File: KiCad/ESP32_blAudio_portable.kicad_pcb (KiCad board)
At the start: 2 copper layers, 102 parts, among them J1 Conn_01x15_Male, J2 Conn_01x15_Male, J3 Conn_01x02_Male, J4 Conn_01x02_Male, J5 Conn_01x02_Male, J7 Conn_01x16_Female, SW1 SW_Push, SW2 SW_Push, SW3 SW_Push, SW5 SW_Push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

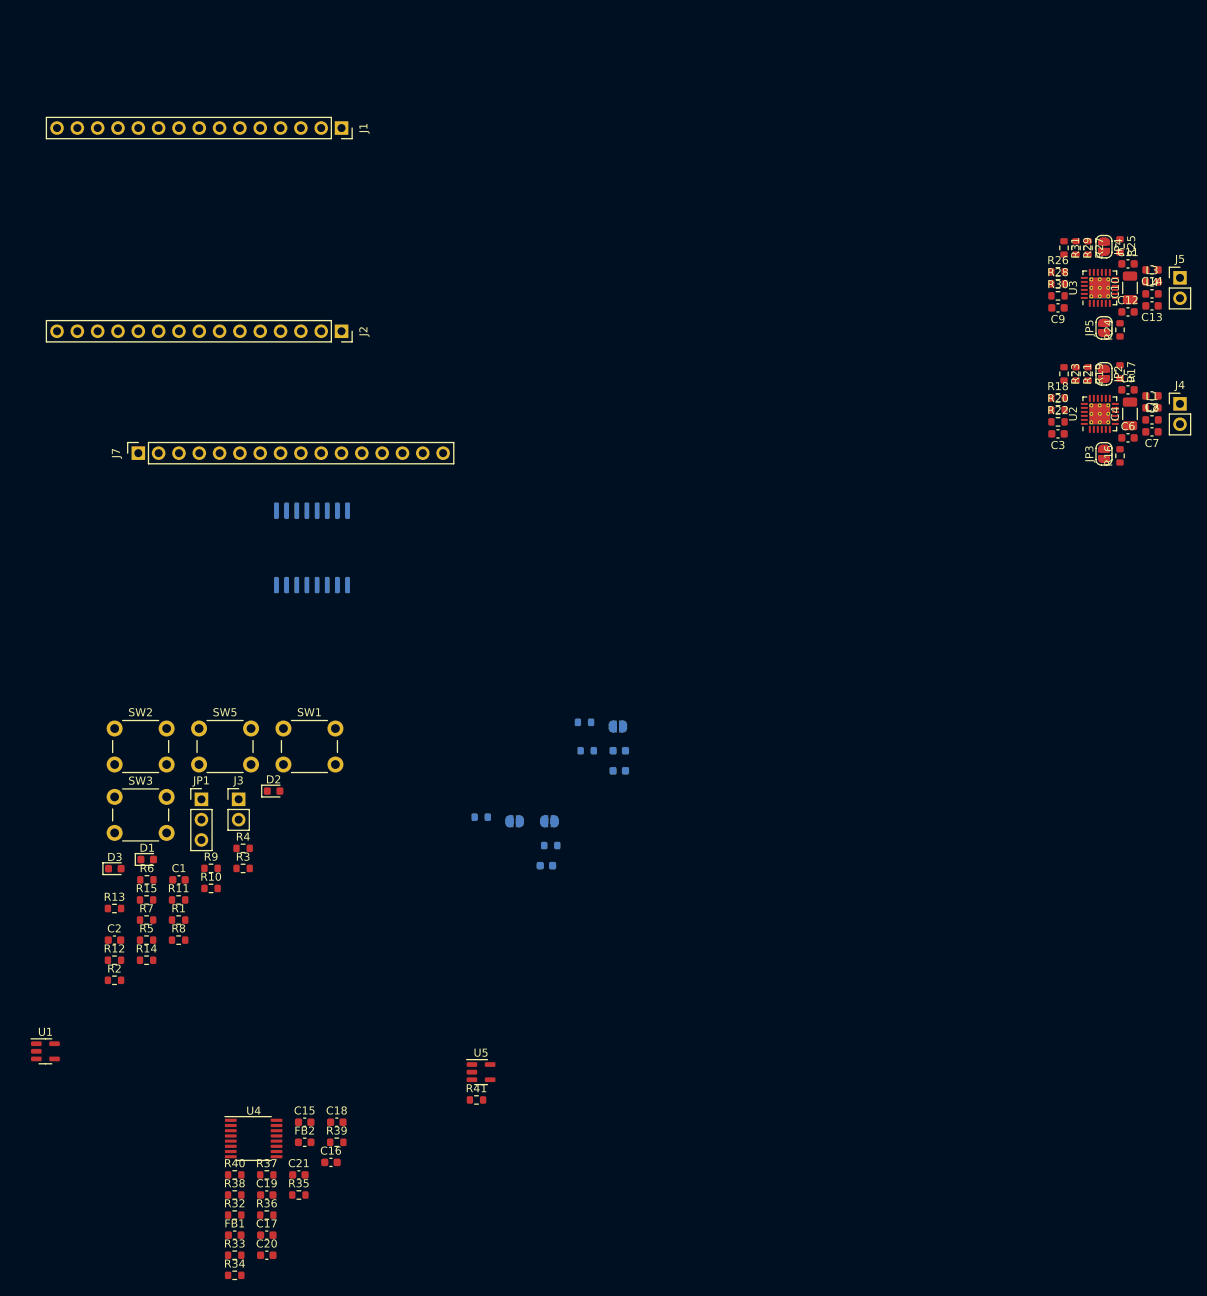
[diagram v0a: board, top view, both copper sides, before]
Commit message: -associated footprints to more specific components -added manufacturer and part series info to more specific components
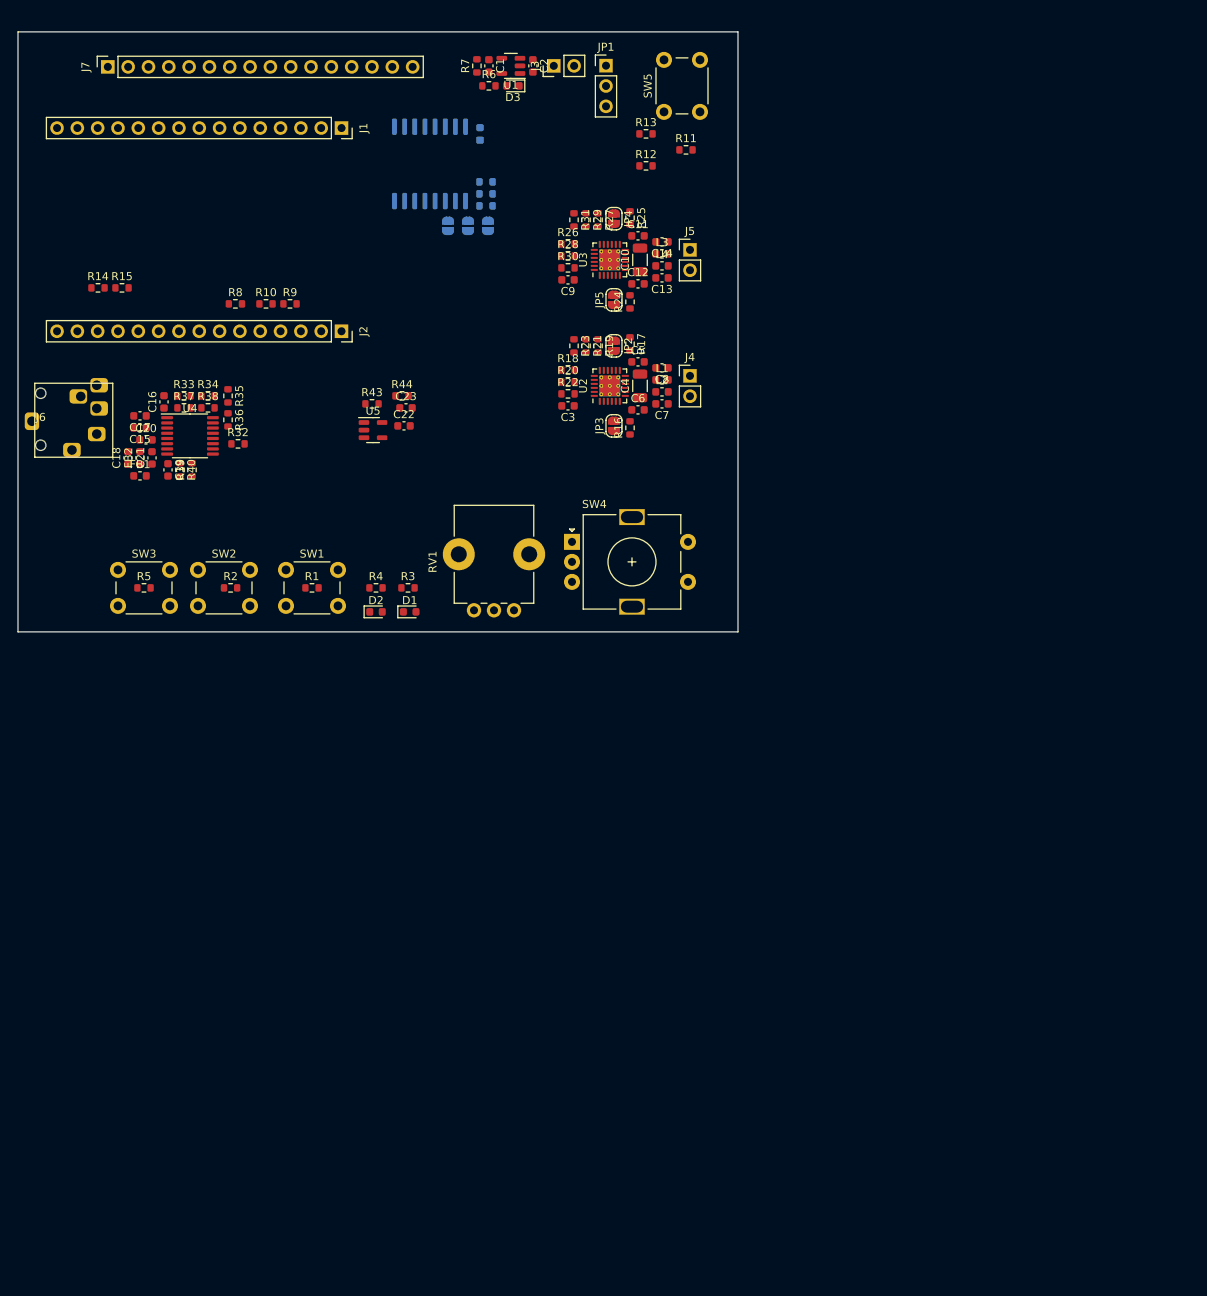
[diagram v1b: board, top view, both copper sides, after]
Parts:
- added J6: ASJ-99H, custom_footprints:ASJ-99H, F.Cu at (53.8, 69.7)
- added RV1: PT01, Potentiometer_THT:Potentiometer_Bourns_PTV09A-1_Single_Vertical, F.Cu at (113.0, 93.3)
- added SW4: PEC12R, Rotary_Encoder:RotaryEncoder_Alps_EC11E-Switch_Vertical_H20mm, F.Cu at (120.2, 84.8)
- C1, C2: value C -> 1u
- C22, C23: value C -> 1u; moved to F.Cu
- R41: moved to B.Cu
- R43, R44: moved to F.Cu
- SW1, SW2, SW3, SW5: value SW_Push -> TS02
- moved U1 136.2 mm to (112.6, 25.2), turned to 180 degrees
- moved C2 121.2 mm to (115.4, 25.2), turned to -90 degrees
- moved R12 119.5 mm to (129.5, 37.8)
- moved R13 117.4 mm to (129.5, 33.8)
- moved R7 114.5 mm to (108.4, 25.2), turned to 90 degrees
- moved R11 113.2 mm to (134.5, 35.8)
- moved R41 111.8 mm to (109.5, 42.8)
- moved R34 110.0 mm to (74.8, 66.5)
- moved D3 109.8 mm to (112.9, 27.8), turned to 180 degrees
- moved C1 108.9 mm to (109.9, 25.2), turned to -90 degrees
- moved R6 108.1 mm to (109.9, 27.8)
- moved R33 107.6 mm to (71.8, 66.5)
- moved JP1 104.7 mm to (124.5, 25.2)
- moved C17 103.6 mm to (66.2, 69.0), turned to 180 degrees
- moved C20 103.0 mm to (67.0, 72.0)
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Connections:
- C15 pad 2: unconnected-(C15-Pad2) -> Net-(J6-PadT)
- C17 pad 2: unconnected-(C17-Pad2) -> Net-(J6-PadR)
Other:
- board outline added: 90 x 75 mm

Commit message: -layout work
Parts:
- removed R10, R8, R9: 22R, Resistor_SMD:R_0603_1608Metric
- moved R36 3.54 mm to (77.8, 66.0), turned to 90 degrees
- moved R32 2.93 mm to (79.5, 69.8)
- moved C15 2.55 mm to (66.8, 68.0)
- moved C16 2.55 mm to (69.8, 64.8)
- moved C17 2.55 mm to (66.8, 66.5)
- moved C18 2.55 mm to (65.2, 71.8)
- moved C19 2.55 mm to (70.2, 73.2)
- moved C20 2.55 mm to (67.5, 69.5)
- moved C21 2.55 mm to (68.2, 71.8)
- moved FB1 2.55 mm to (66.8, 74.0)
- moved FB2 2.55 mm to (66.8, 71.8)
- moved R33 2.55 mm to (72.2, 64.0)
- moved R34 2.55 mm to (75.2, 64.0)
- moved R37 2.55 mm to (72.2, 65.5)
- moved R38 2.55 mm to (75.2, 65.5)
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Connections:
- J1 pad 14: unconnected-(J1-Pad14) -> GND
- J2 pad 1: unconnected-(J2-Pad1) -> /SDI2
- J2 pad 14: unconnected-(J2-Pad14) -> GND
- J2 pad 2: unconnected-(J2-Pad2) -> /LRCK2
- J2 pad 3: unconnected-(J2-Pad3) -> /MCLK
- J2 pad 4: unconnected-(J2-Pad4) -> /SCK2
- J2 pad 5: unconnected-(J2-Pad5) -> /~{PDN}
- R19 pad 1: /AK5720/SDOUT -> /SDI2
- R21 pad 1: /AK5720/SDCLK -> /SCK2
- R23 pad 1: /AK5720/SDWS -> /LRCK2
- R27 pad 1: /AK5720/SDOUT -> /SDI2
- R29 pad 1: /AK5720/SDCLK -> /SCK2
- R31 pad 1: /AK5720/SDWS -> /LRCK2
- U4 pad 10: /AK5720/SDWS -> /LRCK2
- U4 pad 12: /AK5720/SDCLK -> /SCK2
- U4 pad 9: /AK5720/SDOUT -> /SDI2

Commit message: -layout work
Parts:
- added C25: 1u, Capacitor_SMD:C_0603_1608Metric, F.Cu at (126.1, 36.3)
- added C26: 1u, Capacitor_SMD:C_0603_1608Metric, F.Cu at (126.1, 39.3)
- added D4: 30V 1A, Diode_SMD:D_SOD-323, F.Cu at (100.2, 59.2)
- added L5: 33u, Inductor_SMD:L_Taiyo-Yuden_NR-50xx, F.Cu at (104.0, 65.2)
- added Q1: 2N7002, Package_TO_SOT_SMD:SOT-323_SC-70, F.Cu at (127.8, 33.0)
- added Q2: Q_PMOS_DGS, Package_TO_SOT_SMD:SOT-23-6, F.Cu at (122.0, 28.8)
- added Q3: 2N7002, Package_TO_SOT_SMD:SOT-323_SC-70, F.Cu at (99.5, 29.8)
- added RV2: TC33X_10k, Custom:trimmer_Bourns_tc33x, B.Cu at (64.0, 28.8)
- added U7: NCP1117-3.3_SOT223, Package_TO_SOT_SMD:SOT-223-3_TabPin2, F.Cu at (120.8, 37.8)
- R1, R14, R15, R2, R5: moved to B.Cu
- moved R14 26.1 mm to (81.2, 36.5), turned to 90 degrees
- moved R15 25.7 mm to (83.8, 36.5), turned to 90 degrees
- moved R3 14.4 mm to (90.8, 79.2), turned to 90 degrees
- moved R12 14.2 mm to (122.0, 25.8)
- moved R4 14.1 mm to (87.2, 79.2), turned to 90 degrees
- moved D1 14.0 mm to (90.8, 83.0), turned to 90 degrees
- moved D2 13.5 mm to (87.2, 83.0), turned to 90 degrees
- moved R1 12.6 mm to (78.5, 82.0), turned to 180 degrees
- moved R2 12.6 mm to (68.3, 82.0), turned to 180 degrees
- moved R5 12.6 mm to (57.5, 82.0), turned to 180 degrees
- moved RV1 12.6 mm to (103.8, 84.8)
- moved SW1 12.6 mm to (75.2, 79.8)
- moved SW2 12.6 mm to (64.2, 79.8)
- moved SW3 12.6 mm to (54.2, 79.8)
- moved SW4 12.6 mm to (111.0, 76.2)
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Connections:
- C22 pad 1: +3V3 -> +VDC
- J1 pad 1: unconnected-(J1-Pad1) -> +3V3
- J1 pad 2: unconnected-(J1-Pad2) -> /PWR_ON
- J1 pad 3: unconnected-(J1-Pad3) -> /EN_5V
- J1 pad 4: unconnected-(J1-Pad4) -> /SCL
- J1 pad 5: unconnected-(J1-Pad5) -> /SDA
- J1 pad 6: unconnected-(J1-Pad6) -> /ENC_SW
- J1 pad 7: unconnected-(J1-Pad7) -> /ENC_A
- J1 pad 8: unconnected-(J1-Pad8) -> /ENC_B
- J1 pad 9: unconnected-(J1-Pad9) -> /ANA_VOL
- J2 pad 10: unconnected-(J2-Pad10) -> /LED2
- J2 pad 11: unconnected-(J2-Pad11) -> /BTTN1
- J2 pad 12: unconnected-(J2-Pad12) -> /BTTN2
- J2 pad 13: unconnected-(J2-Pad13) -> /BTTN3
- J2 pad 15: unconnected-(J2-Pad15) -> +3V3
- J2 pad 6: unconnected-(J2-Pad6) -> /LRCK1
- J2 pad 7: unconnected-(J2-Pad7) -> /SCK1
- J2 pad 8: unconnected-(J2-Pad8) -> /SDI1
- J2 pad 9: unconnected-(J2-Pad9) -> /LED1
- U5 pad 5: +3V3 -> +VDC
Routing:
- net /SDI2: track 0.00 -> 71.6 mm, vias 0 -> 3
- net /SCK2: track 0.00 -> 69.3 mm, vias 0 -> 1
- net /LRCK2: track 0.00 -> 64.8 mm, vias 0 -> 1
- net /SDI1: track 0.00 -> 58.8 mm, vias 0 -> 2
- net /SCK1: track 0.00 -> 56.4 mm, vias 0 -> 2
- net /LRCK1: track 0.00 -> 53.8 mm, vias 0 -> 2
- net /Display/LCD_RS: track 0.00 -> 38.2 mm
- net /Display/LCD_R/~{W}: track 0.00 -> 36.0 mm, vias 0 -> 1
- net /Display/LCD_E: track 0.00 -> 32.6 mm, vias 0 -> 1
- net GND: track 0.00 -> 31.1 mm, vias 0 -> 4
- net /BTTN3: track 0.00 -> 18.3 mm
- net +3V3: track 0.00 -> 15.3 mm, vias 0 -> 1
- net /~{PDN}: track 0.00 -> 14.1 mm
- net Net-(C17-Pad2): track 0.00 -> 13.7 mm
- net /MCLK: track 0.00 -> 13.5 mm
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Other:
- board size 90 x 75 mm -> 82.5 x 65.5 mm

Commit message: -layout largely finished, some finishing touches needed
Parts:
- added REF**: MountingHole_3.2mm_M3, MountingHole:MountingHole_3.2mm_M3, F.Cu at (130.2, 83.2)
- added REF**: MountingHole_3.2mm_M3, MountingHole:MountingHole_3.2mm_M3, F.Cu at (54.2, 83.2)
- added REF**: MountingHole_3.2mm_M3, MountingHole:MountingHole_3.2mm_M3, F.Cu at (54.2, 24.2)
- added REF**: MountingHole_3.2mm_M3, MountingHole:MountingHole_3.2mm_M3, F.Cu at (130.2, 39.8)
- Q3: moved to B.Cu
- moved L5 26.5 mm to (104.0, 38.8), turned to 180 degrees
- moved U5 19.3 mm to (104.0, 43.2)
- moved D4 19.2 mm to (100.2, 40.0), turned to 90 degrees
- moved C22 18.7 mm to (106.8, 43.0), turned to -90 degrees
- moved R43 16.3 mm to (99.0, 42.2)
- moved C23 16.1 mm to (101.2, 43.0), turned to -90 degrees
- moved R44 14.1 mm to (99.0, 43.8), turned to 180 degrees
- moved SW3 11.9 mm to (65.2, 84.2), turned to 180 degrees
- moved SW2 11.7 mm to (75.0, 84.2), turned to 180 degrees
- moved SW1 10.5 mm to (84.8, 84.2), turned to 180 degrees
- moved Q3 6.37 mm to (104.2, 25.5), turned to 180 degrees
- moved R5 5.55 mm to (62.0, 78.8), turned to 0 degrees
- moved R2 4.72 mm to (71.8, 78.8), turned to 0 degrees
- moved R1 4.42 mm to (81.5, 78.8), turned to 0 degrees
- moved R12 2.50 mm to (122.0, 23.2)
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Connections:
- J1 pad 13: unconnected-(J1-Pad13) -> /3-5_SW
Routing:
- net +3V3: track 15.3 -> 371.2 mm, vias 1 -> 8
- net +5V: track 4.44 -> 83.6 mm
- net /SDA: track 0.00 -> 77.6 mm, vias 0 -> 4
- net /SCL: track 0.00 -> 75.4 mm, vias 0 -> 4
- net /ENC_SW: track 0.00 -> 72.9 mm, vias 0 -> 1
- net +VDC: track 0.00 -> 68.2 mm, vias 0 -> 9
- net /ANA_VOL: track 0.00 -> 66.0 mm, vias 0 -> 1
- net /ENC_B: track 0.00 -> 65.8 mm, vias 0 -> 1
- net /ENC_A: track 0.00 -> 60.2 mm, vias 0 -> 1
- net +5C: track 3.55 -> 56.4 mm, vias 0 -> 1
- net /PWR_ON: track 0.00 -> 43.0 mm, vias 0 -> 2
- net GND: track 31.1 -> 73.5 mm, vias 4 -> 9
- net /LED1: track 0.00 -> 36.3 mm, vias 0 -> 1
- net /BTTN1: track 0.00 -> 36.0 mm
- net /LED2: track 0.00 -> 34.8 mm, vias 0 -> 1
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- added copper zone on F.Cu, net +VDC
- added copper zone on B.Cu, net GND
- added copper zone on F.Cu, net GND

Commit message: -First board version ready to order
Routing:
- net /SDI2: track 71.3 -> 70.6 mm
- net /LRCK1: track 53.8 -> 54.4 mm
- net GND: vias 9 -> 117
